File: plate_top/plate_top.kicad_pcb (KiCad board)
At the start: 2 copper layers, 157.5 x 118.1 mm, 31 parts, among them SW1 SW_Push

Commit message: Cuts
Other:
- outline, holes or cut-outs redrawn

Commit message: WIP
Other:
- outline, holes or cut-outs redrawn

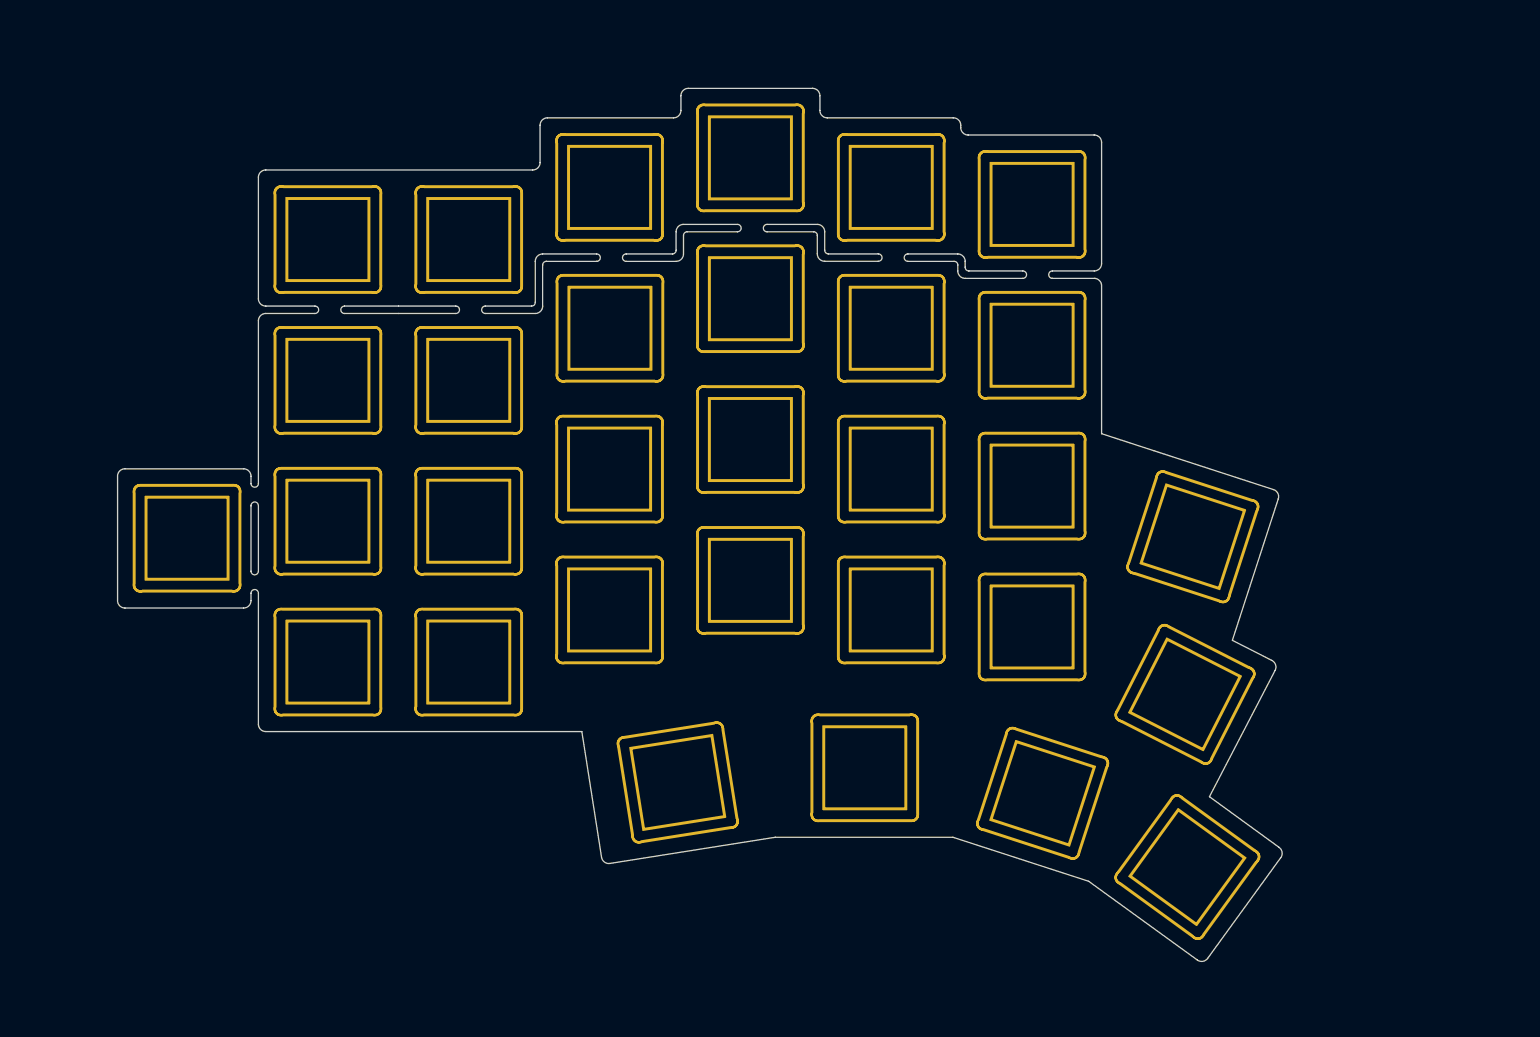
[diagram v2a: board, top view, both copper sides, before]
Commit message: Fixed cut edges + filled zones on plates.
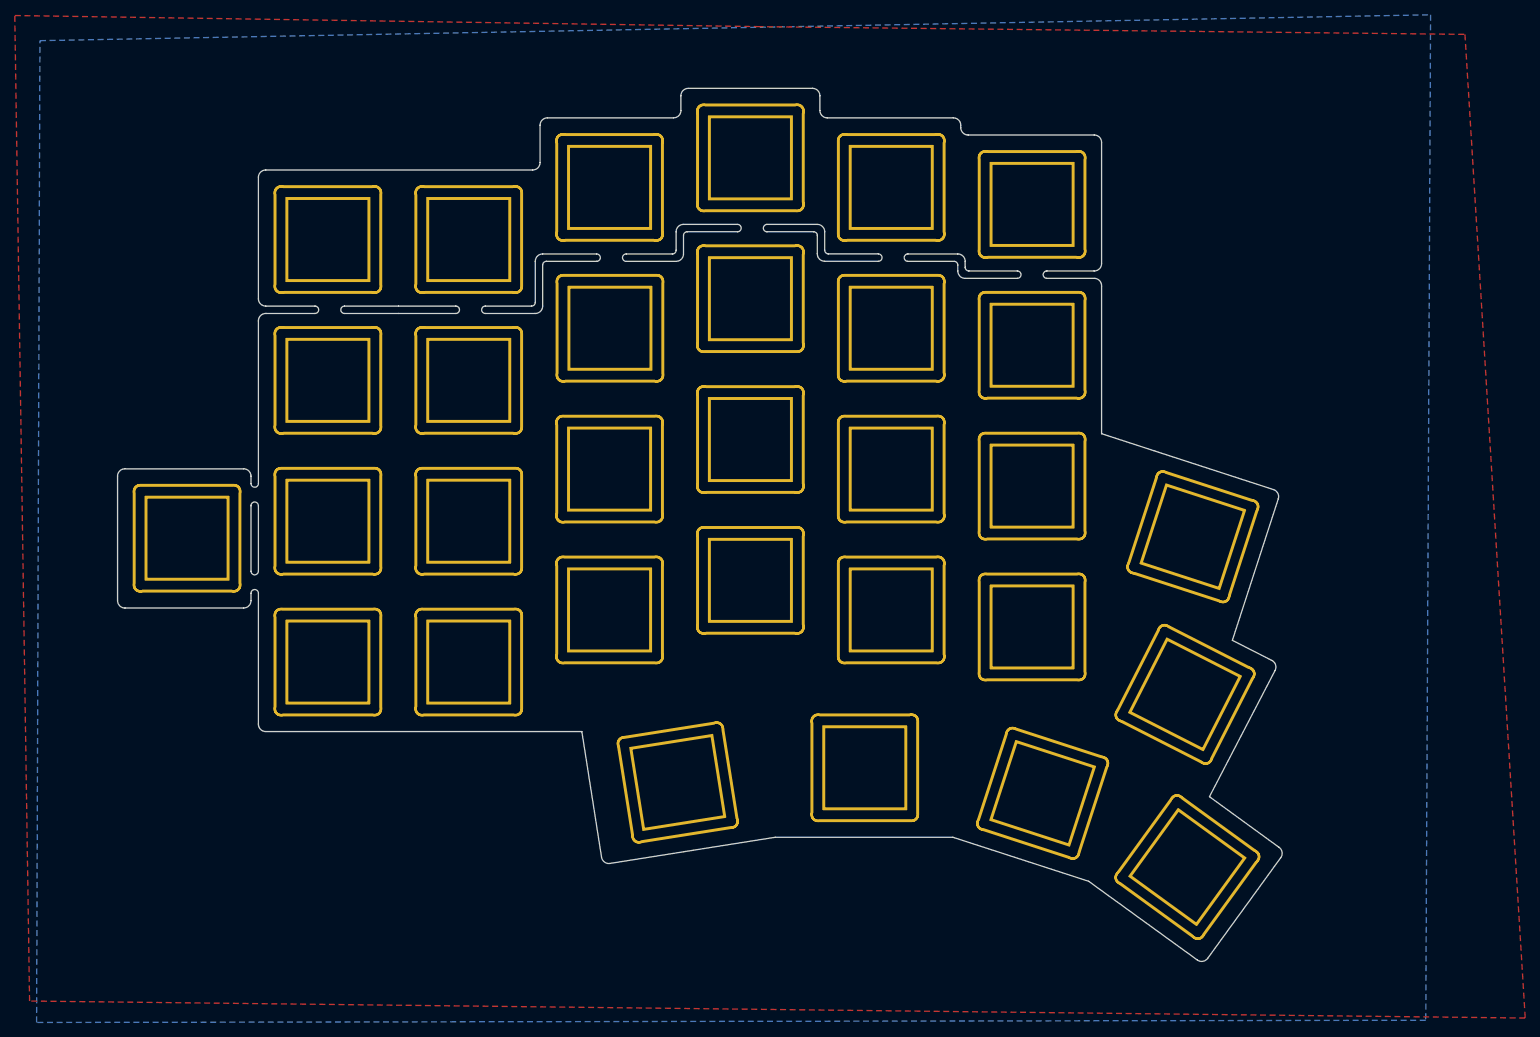
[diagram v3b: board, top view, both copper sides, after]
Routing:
- added copper zone on B.Cu, net (none)
- added copper zone on F.Cu, net (none)
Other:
- outline, holes or cut-outs redrawn
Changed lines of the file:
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@@
     (pad "" thru_hole oval (at 6.35 -0.01 90) (size 14.7 2) (drill oval 13.9 1.2) (layers *.Cu *.Mask))
   )
+  (gr_line (start 191.2 56.25) (end 198.25 56.25) (layer Edge.Cuts) (width 0.05))
+  (gr_arc (start 202.25 55.749999) (end 202.25 55.25) (angle -180) (layer Edge.Cuts) (width 0.05))
+  (gr_arc (start 198.25 55.749998) (end 198.25 56.249996) (angle -180) (layer Edge.Cuts) (width 0.05))
+  (gr_line (start 191.7 55.25) (end 198.25 55.25) (layer Edge.Cuts) (width 0.05))
+  (gr_line (start 208.65 55.25) (end 202.25 55.25) (layer Edge.Cuts) (width 0.05))
   (gr_arc (start 77.55 83.01) (end 77.55 82.01) (angle -90) (layer Edge.Cuts) (width 0.05))
   (gr_arc (start 93.600001 83.01) (end 94.600001 83.01) (angle -90) (layer Edge.Cuts) (width 0.05))
@@
   (gr_line (start 94.600001 83.01) (end 94.600001 84.01) (layer Edge.Cuts) (width 0.05))
   (gr_line (start 76.55 99.84) (end 76.55 83.01) (layer Edge.Cuts) (width 0.05))
-  (gr_arc (start 95.099999 87) (end 95.599997 86.99) (angle -180) (layer Edge.Cuts) (width 0.05))
+  (gr_arc (start 95.099999 87) (end 95.6 87) (angle -181.1457605) (layer Edge.Cuts) (width 0.05))
   (gr_line (start 94.600001 95.849999) (end 94.600001 87.01) (layer Edge.Cuts) (width 0.05))
   (gr_line (start 95.6 87) (end 95.599999 95.850001) (layer Edge.Cuts) (width 0.05))
@@
   (gr_line (start 152.75 31.55) (end 152.75 33.54) (layer Edge.Cuts) (width 0.05))
   (gr_line (start 103.25 61) (end 96.6 61.000001) (layer Edge.Cuts) (width 0.05))
-  (gr_line (start 208.65 55.25) (end 203 55.25) (layer Edge.Cuts) (width 0.05))
   (gr_line (start 95.599998 98.84) (end 95.6 116.55) (layer Edge.Cuts) (width 0.05))
   (gr_arc (start 132.7 40.59) (end 132.7 41.59) (angle -90) (layer Edge.Cuts) (width 0.05))
   (gr_arc (start 134.7 35.54) (end 134.7 34.54) (angle -90) (layer Edge.Cuts) (width 0.05))
   (gr_line (start 189.6 34.54) (end 172.55 34.54) (layer Edge.Cuts) (width 0.05))
-  (gr_line (start 191.7 55.25) (end 199 55.25) (layer Edge.Cuts) (width 0.05))
   (gr_line (start 96.6 60) (end 103.25 60.000001) (layer Edge.Cuts) (width 0.05))
   (gr_line (start 133.05 53.950001) (end 133.05 59.5) (layer Edge.Cuts) (width 0.05))
@@
   (gr_arc (start 151.6 52.45) (end 151.6 52.95) (angle -90) (layer Edge.Cuts) (width 0.05))
   (gr_arc (start 133.05 59.999999) (end 133.05 60.999999) (angle -90) (layer Edge.Cuts) (width 0.05))
-  (gr_arc (start 203 55.749999) (end 203 55.25) (angle -180) (layer Edge.Cuts) (width 0.05))
   (gr_arc (start 107.25 60.5) (end 107.25 60.000001) (angle -180) (layer Edge.Cuts) (width 0.05))
   (gr_line (start 171.199999 50.45) (end 171.200001 52.94) (layer Edge.Cuts) (width 0.05))
-  (gr_line (start 203 56.249998) (end 208.71 56.25) (layer Edge.Cuts) (width 0.05))
+  (gr_line (start 202.25 56.249998) (end 208.71 56.25) (layer Edge.Cuts) (width 0.05))
   (gr_line (start 153.1 52.949999) (end 153.100001 50.45) (layer Edge.Cuts) (width 0.05))
   (gr_line (start 153.6 49.95) (end 160.4 49.949997) (layer Edge.Cuts) (width 0.05))
@@
   (gr_line (start 172.200001 53.94) (end 179.45 53.94) (layer Edge.Cuts) (width 0.05))
   (gr_line (start 107.25 61) (end 114.55 61.000001) (layer Edge.Cuts) (width 0.05))
-  (gr_arc (start 199 55.749998) (end 199 56.249996) (angle -180) (layer Edge.Cuts) (width 0.05))
   (gr_line (start 145.35 52.950001) (end 151.6 52.95) (layer Edge.Cuts) (width 0.05))
   (gr_line (start 152.1 52.45) (end 152.1 49.950001) (layer Edge.Cuts) (width 0.05))
@@
   (gr_arc (start 126.3 60.5) (end 126.3 60.000001) (angle -180) (layer Edge.Cuts) (width 0.05))
   (gr_line (start 165.5 131.85) (end 189.55 131.85) (layer Edge.Cuts) (width 0.05))
-  (gr_line (start 191.2 56.25) (end 199 56.249996) (layer Edge.Cuts) (width 0.05))
   (gr_line (start 96.6 41.59) (end 132.7 41.59) (layer Edge.Cuts) (width 0.05))
   (gr_line (start 95.6 59) (end 95.6 42.59) (layer Edge.Cuts) (width 0.05))
@@
   (gr_line (start 208.1 116.75) (end 216.5 120.95) (layer Cmts.User) (width 0.15))
   (gr_line (start 228.309948 97.73809) (end 206.7 140.15) (layer Cmts.User) (width 0.15))
+  (zone (net 0) (net_name "") (layer F.Cu) (hatch edge 0.508)
+    (connect_pads (clearance 0.508))
+    (min_thickness 0.254)
+    (fill yes (arc_segments 32) (thermal_gap 0.508) (thermal_bridge_width 0.508))
+    (polygon
+      (pts
+        (xy 163.1 22.2) (xy 258.8 23.25) (xy 266.95 156.3) (xy 64.65 154) (xy 62.65 20.7)
+      )
+    )
+  )
+  (zone (net 0) (net_name "") (layer B.Cu) (hatch edge 0.508)
+    (connect_pads (clearance 0.508))
+    (min_thickness 0.254)
+    (fill yes (arc_segments 32) (thermal_gap 0.508) (thermal_bridge_width 0.508))
+    (polygon
+      (pts
+        (xy 253.5 156.6) (xy 65.6 156.9) (xy 66.05 24.1) (xy 254.15 20.6)
+      )
+    )
+  )
 )

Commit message: Using different cutout footprints
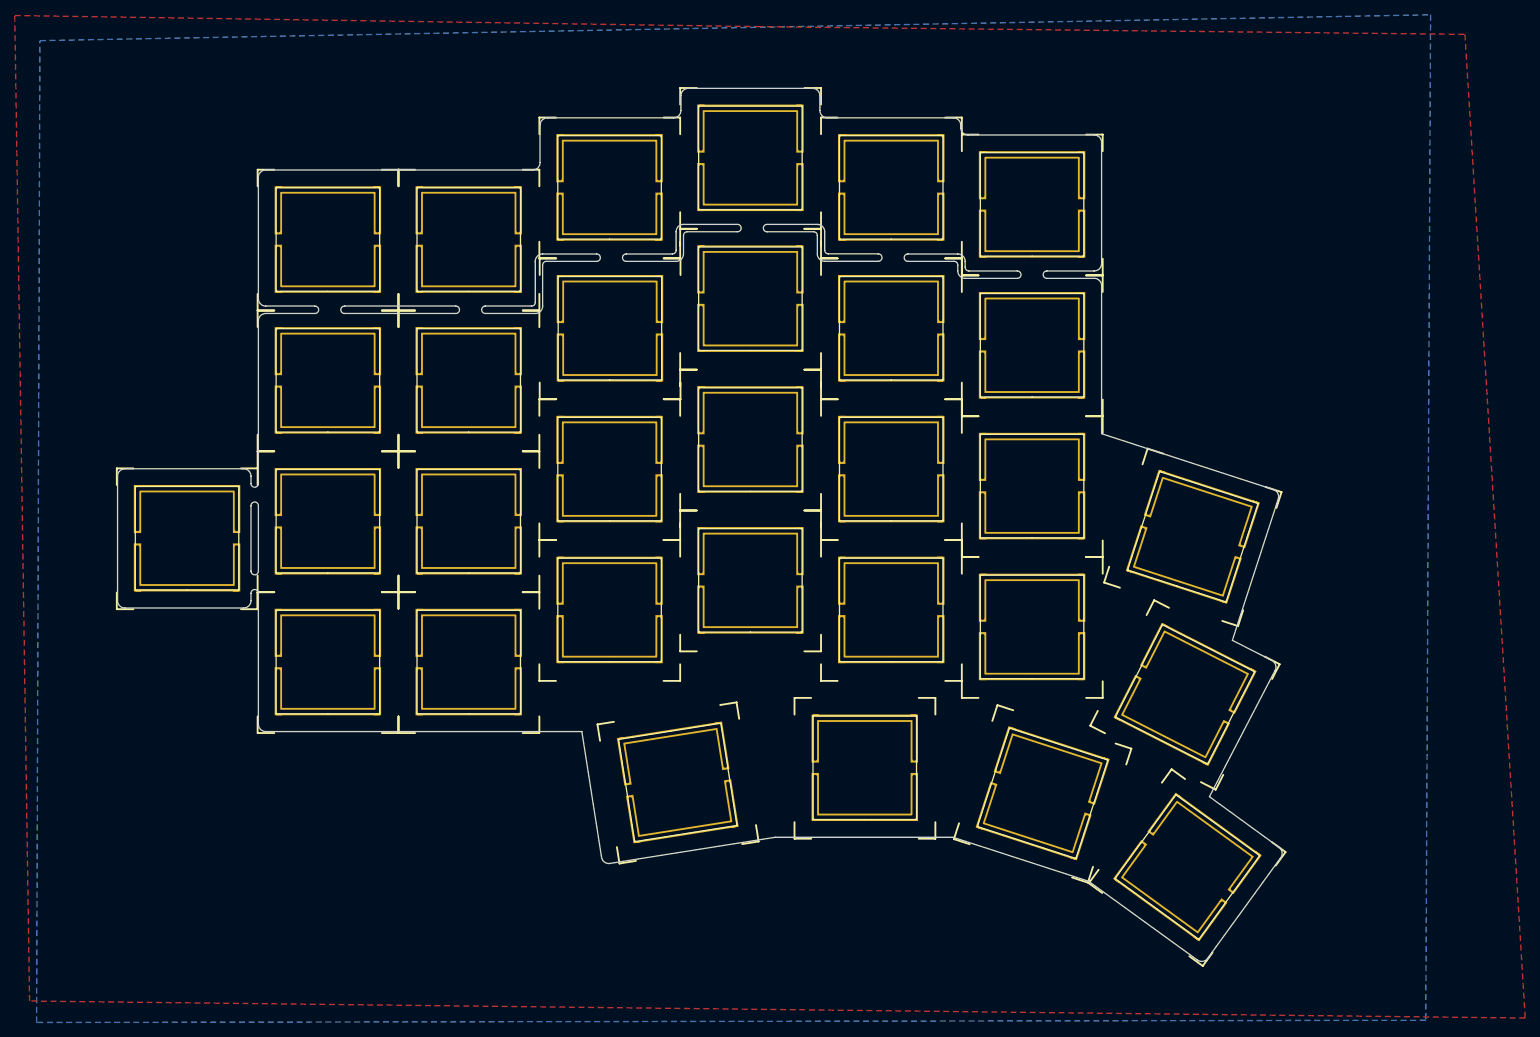
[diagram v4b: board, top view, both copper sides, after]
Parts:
- removed the SW1 at (221.3, 135.9)
- removed the SW1 at (200.2, 65.3)
- removed the SW1 at (200.2, 46.2)
- removed the SW1 at (181.2, 101.1)
- removed the SW1 at (181.2, 82.0)
- removed the SW1 at (181.2, 63.0)
- removed the SW1 at (181.2, 44.0)
- removed the SW1 at (162.2, 40.0)
- removed the SW1 at (162.2, 59.0)
- removed the SW1 at (162.2, 78.0)
- removed the SW1 at (162.2, 97.1)
- removed the SW1 at (201.7, 125.9)
- removed the SW1 at (143.1, 101.1)
- removed the SW1 at (143.1, 82.0)
- removed the SW1 at (143.2, 63.0)
- removed the SW1 at (143.1, 44.0)
- removed the SW1 at (124.0, 51.0)
- removed the SW1 at (124.0, 70.0)
- removed the SW1 at (124.0, 89.1)
- removed the SW1 at (124.0, 108.2)
- removed the SW1 at (105.0, 108.2)
- removed the SW1 at (86.0, 91.4)
- removed the SW1 at (177.6, 122.5)
- removed the SW1 at (105.0, 70.0)
- removed the SW1 at (152.3, 124.4)
- removed the SW1 at (105.0, 89.1)
- removed the SW1 at (200.2, 103.4)
- removed the SW1 at (200.2, 84.3)
- added SW1: SW_Push, used_footprints:metallized_breakout_cutout, F.Cu at (221.3, 135.9)
- added SW1: SW_Push, used_footprints:metallized_breakout_cutout, F.Cu at (200.2, 65.3)
- added SW1: SW_Push, used_footprints:metallized_breakout_cutout, F.Cu at (200.2, 46.2)
- added SW1: SW_Push, used_footprints:metallized_breakout_cutout, F.Cu at (181.2, 101.1)
- added SW1: SW_Push, used_footprints:metallized_breakout_cutout, F.Cu at (181.2, 82.0)
- added SW1: SW_Push, used_footprints:metallized_breakout_cutout, F.Cu at (181.2, 63.0)
- added SW1: SW_Push, used_footprints:metallized_breakout_cutout, F.Cu at (181.2, 44.0)
- added SW1: SW_Push, used_footprints:metallized_breakout_cutout, F.Cu at (162.2, 40.0)
- added SW1: SW_Push, used_footprints:metallized_breakout_cutout, F.Cu at (162.2, 59.0)
- added SW1: SW_Push, used_footprints:metallized_breakout_cutout, F.Cu at (162.2, 78.0)
- added SW1: SW_Push, used_footprints:metallized_breakout_cutout, F.Cu at (162.2, 97.1)
- added SW1: SW_Push, used_footprints:metallized_breakout_cutout, F.Cu at (201.7, 125.9)
- added SW1: SW_Push, used_footprints:metallized_breakout_cutout, F.Cu at (143.1, 101.1)
- added SW1: SW_Push, used_footprints:metallized_breakout_cutout, F.Cu at (143.1, 82.0)
- added SW1: SW_Push, used_footprints:metallized_breakout_cutout, F.Cu at (143.2, 63.0)
- added SW1: SW_Push, used_footprints:metallized_breakout_cutout, F.Cu at (143.1, 44.0)
- added SW1: SW_Push, used_footprints:metallized_breakout_cutout, F.Cu at (124.0, 51.0)
- added SW1: SW_Push, used_footprints:metallized_breakout_cutout, F.Cu at (124.0, 70.0)
- added SW1: SW_Push, used_footprints:metallized_breakout_cutout, F.Cu at (124.0, 89.1)
- added SW1: SW_Push, used_footprints:metallized_breakout_cutout, F.Cu at (124.0, 108.2)
- added SW1: SW_Push, used_footprints:metallized_breakout_cutout, F.Cu at (105.0, 108.2)
- added SW1: SW_Push, used_footprints:metallized_breakout_cutout, F.Cu at (86.0, 91.4)
- added SW1: SW_Push, used_footprints:metallized_breakout_cutout, F.Cu at (177.6, 122.5)
- added SW1: SW_Push, used_footprints:metallized_breakout_cutout, F.Cu at (105.0, 70.0)
- added SW1: SW_Push, used_footprints:metallized_breakout_cutout, F.Cu at (152.3, 124.4)
- added SW1: SW_Push, used_footprints:metallized_breakout_cutout, F.Cu at (105.0, 89.1)
- added SW1: SW_Push, used_footprints:metallized_breakout_cutout, F.Cu at (200.2, 103.4)
- added SW1: SW_Push, used_footprints:metallized_breakout_cutout, F.Cu at (200.2, 84.3)
- SW1 (x3): footprint used_footprints:TopPlateCutout -> used_footprints:metallized_breakout_cutout

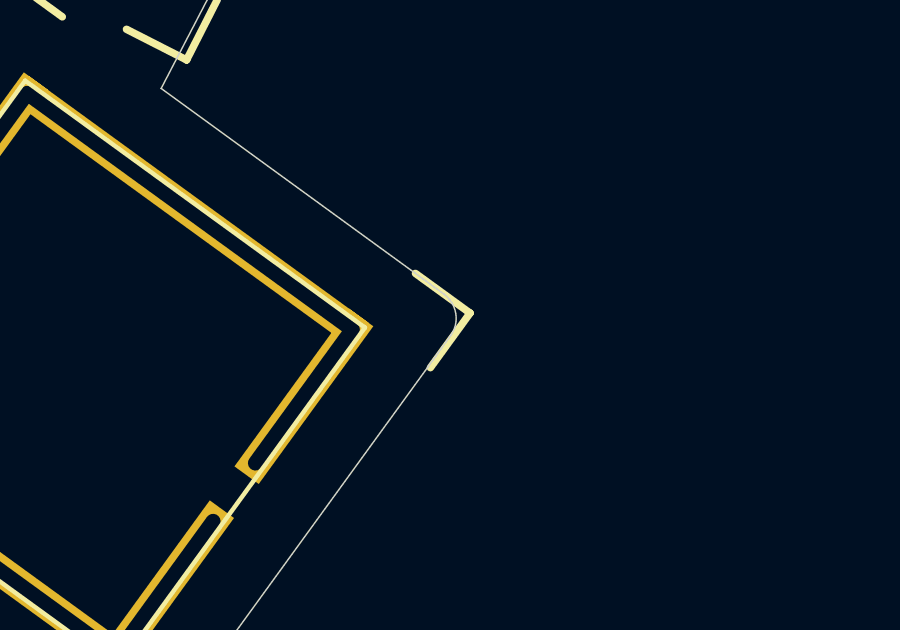
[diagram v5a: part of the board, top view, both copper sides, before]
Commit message: Reduced width of the top plate for 0.05mm
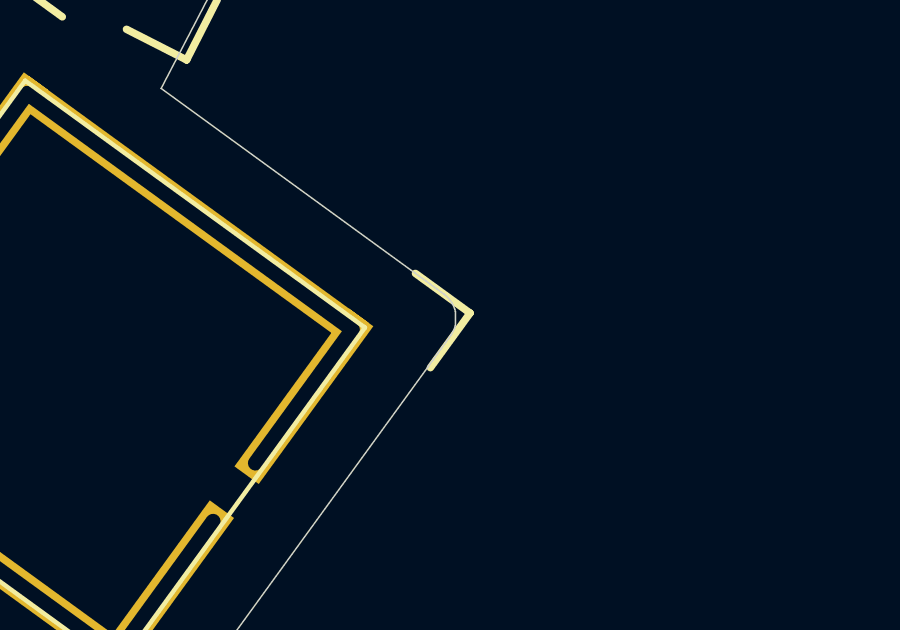
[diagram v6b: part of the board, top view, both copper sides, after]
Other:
- outline, holes or cut-outs redrawn
